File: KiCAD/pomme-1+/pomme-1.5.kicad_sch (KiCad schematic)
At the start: 34 parts, among them J6 clock select, SW1 RESET, U12 74HC138, U2 74HC04, U3 74HC74, U7 74HC00, Y1 3.6864Mhz

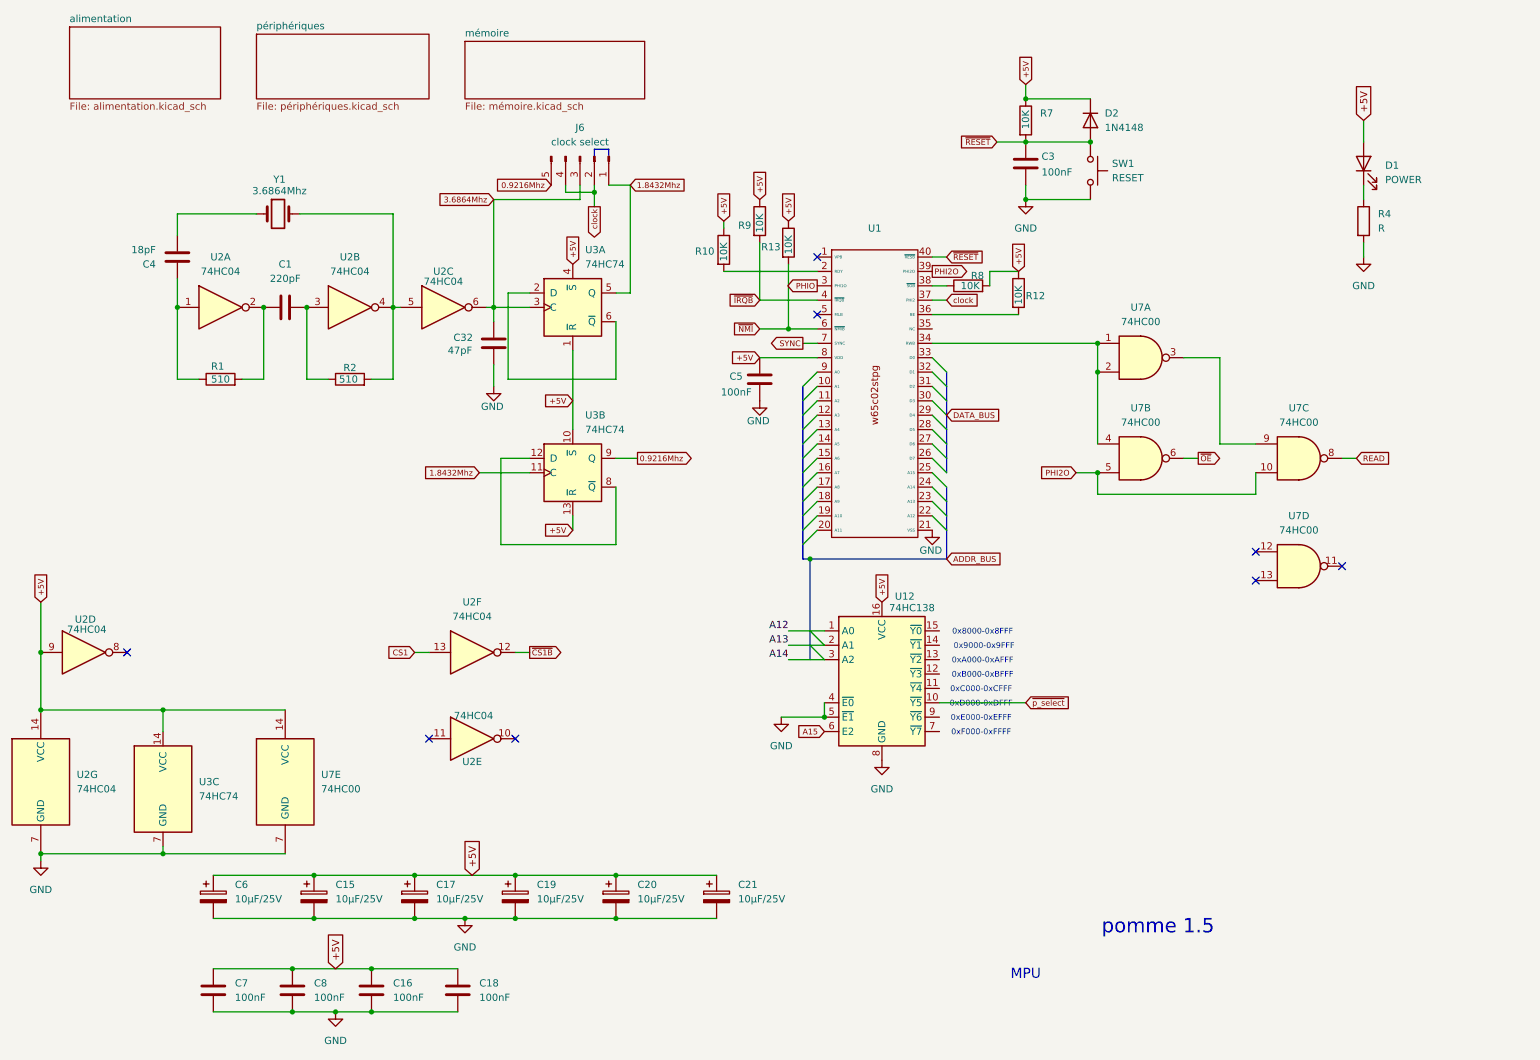
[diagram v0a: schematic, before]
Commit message: Modification de la conception du pomme 1+ Ajout d'un PIA W65C22 à la carte périphériques Ajout d'un régulateur de tension 3.3V à l'alimentation
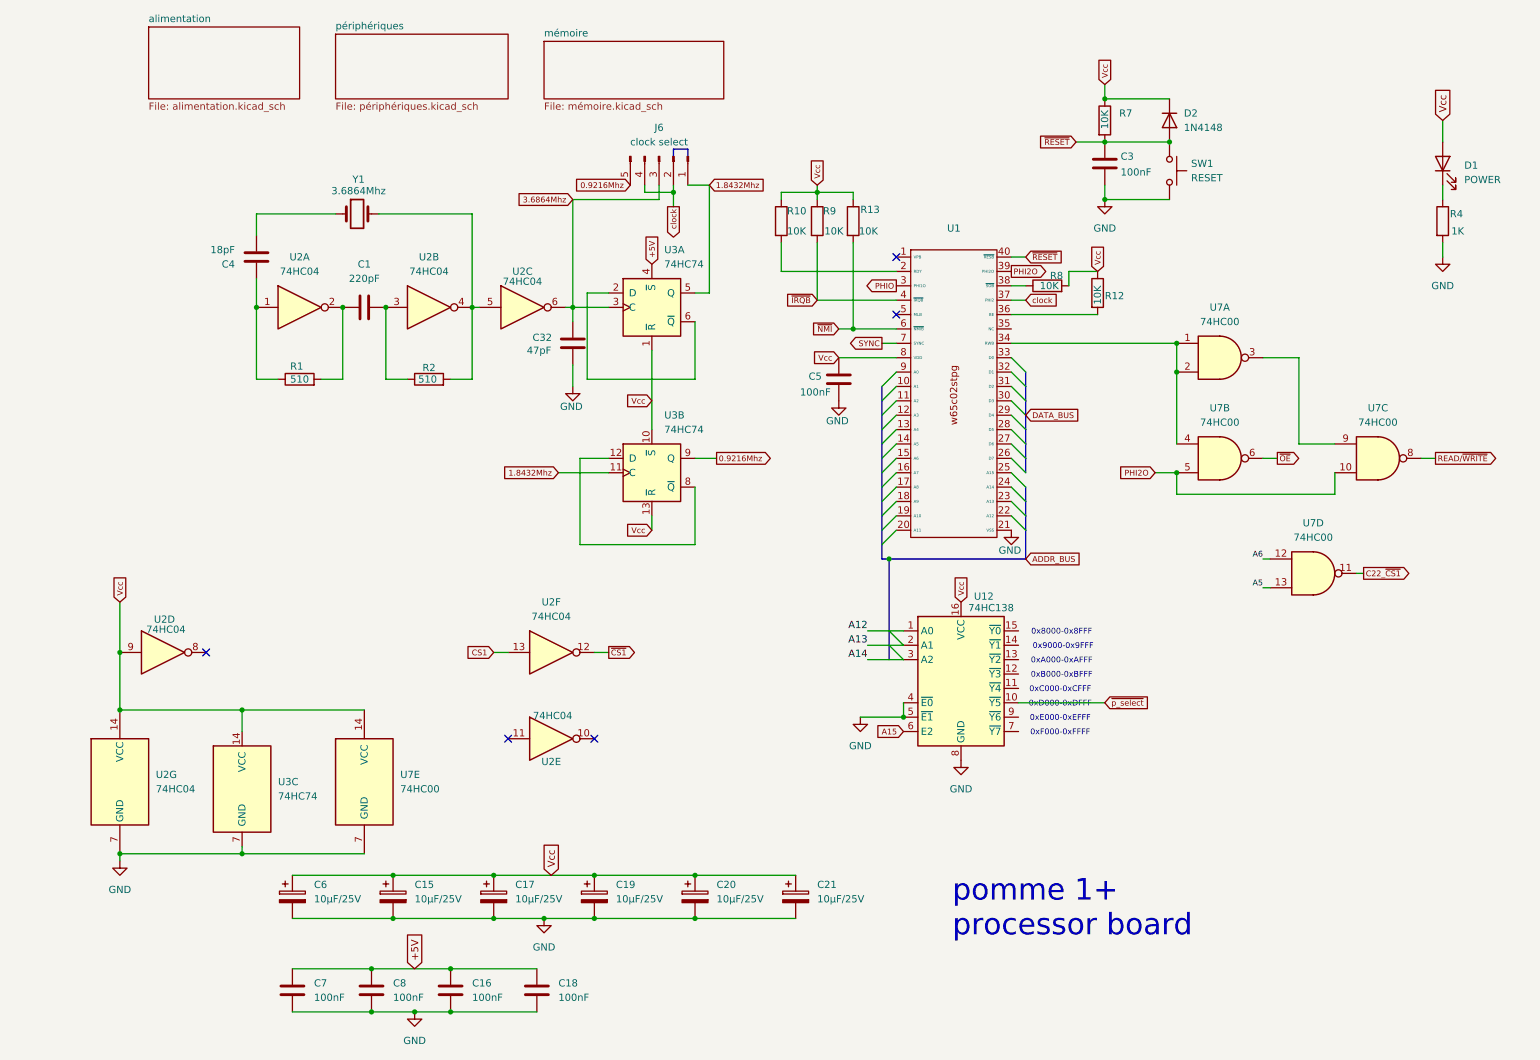
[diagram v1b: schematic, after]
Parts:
- R4: value R -> 1K
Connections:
- net +5V: no longer C15.1, C17.1, C19.1, C20.1, C21.1, C5.1, C6.1, D1.2 (A), D2.1 (K), R10.1, R12.1, R13.1, R7.1, R8.2, R9.1, U1.8 (VDD), U12.16 (VCC), U2.14 (VCC), U2.9, U3.1 (~{R}), U3.10 (~{S}), U3.13 (~{R}), U3.14 (VCC), U7.14 (VCC)
- net C22_~{CS1}: now reaches U7.11
- net A6: now reaches U7.12
- net A5: now reaches U7.13
- net READ renamed READ/~{WRITE}
- net ~{CS1B} renamed ~{CS1}
- new net Vcc: C15.1, C17.1, C19.1, C20.1, C21.1, C5.1, C6.1, D1.2 (A), D2.1 (K), R10.1, R12.1, R13.1, R7.1, R8.2, R9.1, U1.8 (VDD), U12.16 (VCC), U2.14 (VCC), U2.9, U3.1 (~{R}), U3.10 (~{S}), U3.13 (~{R}), U3.14 (VCC), U7.14 (VCC)
- no-connect marks 8 -> 5
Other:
- note added: "pomme 1+ processor board"
- note removed: "MPU"
- note removed: "pomme 1.5"
- moved on the sheet: C1, C15, C16, C17, C18, C19, C20, C21, C3, C32, C4, C5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

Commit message: Modification documents
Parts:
- renumbered C4 to C1, C32 to C10, C19 to C11, C20 to C12, C21 to C13, C5 to C14, C3 to C15, C6 to C2, C7 to C3, C1 to C4, C8 to C5, C15 to C6, C16 to C7, C17 to C8, C18 to C9, D2 to D1, D1 to D2, J6 to J1, R10 to R3, R9 to R4, R13 to R5, R8 to R6, R12 to R7, R7 to R8, R4 to R9, U2 to U1, U3 to U2, U7 to U3, U1 to U4, U12 to U5

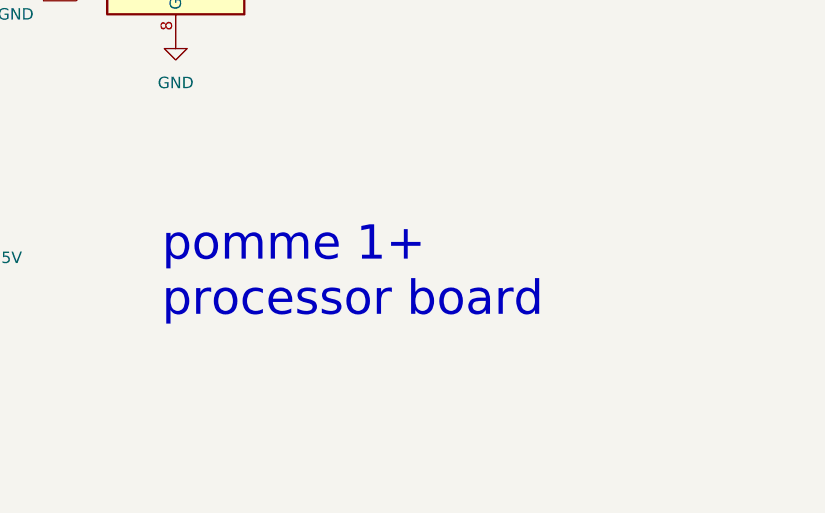
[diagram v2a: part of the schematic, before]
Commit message: Création d'une carte avec mémoire flash W25Q080DV de 1MO pour le stockage des fichiers du pomme 1+
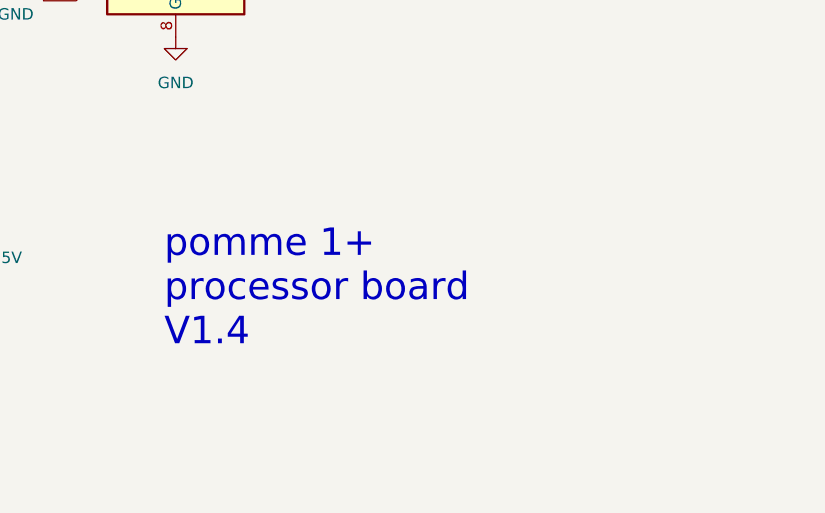
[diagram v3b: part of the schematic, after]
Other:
- note added: "pomme 1+ processor board V1.4"
- note removed: "pomme 1+ processor board"
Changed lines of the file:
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@@
 		)
 	)
-	(text "pomme 1+\nprocessor board\n"
+	(text "pomme 1+\nprocessor board\nV1.4"
 		(exclude_from_sim no)
-		(at 178.816 172.212 0)
+		(at 179.07 173.99 0)
 		(effects
 			(font
-				(size 3.81 3.81)
+				(size 3.048 3.048)
 			)
 			(justify left)

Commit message: Modification schématique V1.5
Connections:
- net C22_~{CS1} renamed C22_~{CS2}
- net ~{CS1} renamed C51_~{CS1}
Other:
- note added: "pomme 1+ processor board V1.5"
- note removed: "pomme 1+ processor board V1.4"
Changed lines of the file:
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@@
 		)
 	)
-	(text "pomme 1+\nprocessor board\nV1.4"
+	(text "pomme 1+\nprocessor board\nV1.5"
 		(exclude_from_sim no)
 		(at 179.07 173.99 0)
@@
 		)
 	)
-	(global_label "C22_~{CS1}"
+	(global_label "C22_~{CS2}"
 		(shape output)
 		(at 251.46 113.03 0)
@@
 		)
 	)
-	(global_label "~{CS1}"
+	(global_label "C51_~{CS1}"
 		(shape output)
 		(at 118.11 127 0)
@@
 		)
 		(property "Intersheetrefs" "${INTERSHEET_REFS}"
-			(at 123.4491 127 0)
-			(effects
-				(font
+			(at 127.1744 127 0)
+			(effects
+				(font

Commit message: Schematic V1.6, modifié circuit pin 12 de U3D pour que la sortie du NAND ne passe à 0 qui si C22_CS1 est à 1
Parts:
- added D7, D8: 1N4148, Diode_THT:D_DO-35_SOD27_P7.62mm_Horizontal, symbol Diode:1N4148
- added R13: 10K, symbol Device:R
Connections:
- net A6: now also D7.1 (K); no longer U3.12
- net Vcc: now also R13.1
- new net: D7.2 (A), D8.2 (A), R13.2, U3.12
- new net C22_CS1: D8.1 (K)
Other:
- note added: "pomme 1+ processor board V1.6"
- note removed: "pomme 1+ processor board V1.5"

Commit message: Correction à la schématique les W65C51S et W65C22S doivent revevoir le signal RWB du mpu plutôt que le signal READ/WRITEB à la pin 8 de U3
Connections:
- net PHI2O: no longer U3.10, U3.5
- net R/~{W}: now reaches U3.1, U3.2, U3.4, U4.34 (RWB)
- new net PHI2: U3.10, U3.5
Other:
- note added: "pomme 1+ processor board V1.8"
- note removed: "pomme 1+ processor board V1.6"
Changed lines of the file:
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@@
+	)
+	(junction
+		(at 200.66 72.39)
+		(diameter 0)
+		(color 0 0 0 0)
 	)
 	(junction
@@
 	(wire
 		(pts
+			(xy 200.66 72.39) (xy 218.44 72.39)
+		)
+		(stroke
+			(width 0)
+			(type default)
+		)
+	)
+	(wire
+		(pts
 			(xy 161.29 69.85) (xy 168.91 69.85)
 		)
@@
 		)
 	)
+	(wire
+		(pts
+			(xy 200.66 72.39) (xy 200.66 74.93)
+		)
+		(stroke
+			(width 0)
+			(type default)
+		)
+	)
 	(bus
 		(pts
@@
 	(wire
 		(pts
-			(xy 189.23 72.39) (xy 218.44 72.39)
+			(xy 189.23 72.39) (xy 200.66 72.39)
 		)
 		(stroke
@@
 		)
 	)
-	(text "pomme 1+\nprocessor board\nV1.6"
+	(text "pomme 1+\nprocessor board\nV1.8"
 		(exclude_from_sim no)
 		(at 179.07 173.99 0)
@@
 		)
 	)
-	(global_label "PHI2O"
+	(global_label "PHI2"
 		(shape input)
 		(at 214.63 95.25 180)
@@
 		)
 		(property "Intersheetrefs" "${INTERSHEET_REFS}"
-			(at 207.6459 95.25 0)
+			(at 208.7103 95.25 0)
 			(effects
 				(font
@@
 				(hide yes)
 			)
+		)
+	)
+	(global_label "R{slash}~{W}"
+		(shape output)
+		(at 200.66 74.93 270)
+		(fields_autoplaced yes)
+		(effects
+			(font
+				(size 1.016 1.016)
+			)
+			(justify right)
+		)
+		(property "Intersheetrefs" "${INTERSHEET_REFS}"
+			(at 200.66 80.5594 90)
+			(effects
+				(font
+					(size 1.27 1.27)
+				)
+				(justify right)
+				(hide yes)
+			)

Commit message: Modification du circuit pour ajouter un amplificateur audio LM4861 sur la carte amovible qui se branche sur le connecteur VIA BUS
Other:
- added sheet carte_ssd_son (carte_ssd_son.kicad_sch)
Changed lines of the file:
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@@
 (kicad_sch
-	(version 20231120)
+	(version 20250114)
 	(generator "eeschema")
-	(generator_version "8.0")
+	(generator_version "9.0")
 	(paper "A4")
+	(text "0x9000-0x9FFF"
+		(exclude_from_sim no)
+		(at 198.374 125.984 0)
+		(effects
+			(font
+				(size 1.016 1.016)
+			)
+		)
+	)
+	(text "pomme 1+\nprocessor board\nV1.8"
+		(exclude_from_sim no)
+		(at 179.07 173.99 0)
+		(effects
+			(font
+				(size 3.048 3.048)
+			)
+			(justify left)
+		)
+	)
+	(text "0xF000-0xFFFF"
+		(exclude_from_sim no)
+		(at 197.866 141.224 0)
+		(effects
+			(font
+				(size 1.016 1.016)
+			)
+		)
+	)
+	(text "0xE000-0xEFFF"
+		(exclude_from_sim no)
+		(at 197.866 138.684 0)
+		(effects
+			(font
+				(size 1.016 1.016)
+			)
+		)
+	)
+	(text "0xD000-0xDFFF"
+		(exclude_from_sim no)
+		(at 197.866 136.144 0)
+		(effects
+			(font
+				(size 1.016 1.016)
+			)
+		)
+	)
+	(text "0xA000-0xAFFF"
+		(exclude_from_sim no)
+		(at 198.12 128.524 0)
+		(effects
+			(font
+				(size 1.016 1.016)
+			)
+		)
+	)
+	(text "0xB000-0xBFFF"
+		(exclude_from_sim no)
+		(at 198.12 131.064 0)
+		(effects
+			(font
+				(size 1.016 1.016)
+			)
+		)
+	)
+	(text "0x8000-0x8FFF"
+		(exclude_from_sim no)
+		(at 198.12 123.444 0)
+		(effects
+			(font
+				(size 1.016 1.016)
+			)
+		)
+	)
+	(text "0xC000-0xCFFF"
+		(exclude_from_sim no)
+		(at 197.866 133.604 0)
+		(effects
+			(font
+				(size 1.016 1.016)
+			)
+		)
+	)
 	(junction
 		(at 161.29 69.85)
@@
 		)
 	)
-	(text "0x9000-0x9FFF"
-		(exclude_from_sim no)
-		(at 198.374 125.984 0)
-		(effects
-			(font
-				(size 1.016 1.016)
-			)
-		)
-	)
-	(text "pomme 1+\nprocessor board\nV1.8"
-		(exclude_from_sim no)
-		(at 179.07 173.99 0)
-		(effects
-			(font
-				(size 3.048 3.048)
-			)
-			(justify left)
-		)
-	)
-	(text "0xF000-0xFFFF"
-		(exclude_from_sim no)
-		(at 197.866 141.224 0)
-		(effects
-			(font
-				(size 1.016 1.016)
-			)
-		)
-	)
-	(text "0xE000-0xEFFF"
-		(exclude_from_sim no)
-		(at 197.866 138.684 0)
-		(effects
-			(font
-				(size 1.016 1.016)
-			)
-		)
-	)
-	(text "0xD000-0xDFFF"
-		(exclude_from_sim no)
-		(at 197.866 136.144 0)
-		(effects
-			(font
-				(size 1.016 1.016)
-			)
-		)
-	)
-	(text "0xA000-0xAFFF"
-		(exclude_from_sim no)
-		(at 198.12 128.524 0)
-		(effects
-			(font
-				(size 1.016 1.016)
-			)
-		)
-	)
-	(text "0xB000-0xBFFF"
-		(exclude_from_sim no)
-		(at 198.12 131.064 0)
-		(effects
-			(font
-				(size 1.016 1.016)
-			)
-		)
-	)
-	(text "0x8000-0x8FFF"
-		(exclude_from_sim no)
-		(at 198.12 123.444 0)
-		(effects
-			(font
-				(size 1.016 1.016)
-			)
-		)
-	)
-	(text "0xC000-0xCFFF"
-		(exclude_from_sim no)
-		(at 197.866 133.604 0)
-		(effects
-			(font
-				(size 1.016 1.016)
-			)
-		)
-	)
 	(label "A6"
 		(at 219.71 110.49 180)
@@
 		(at 36.83 16.51)
 		(size 26.67 12.7)
+		(exclude_from_sim no)
+		(in_bom yes)
+		(on_board yes)
+		(dnp no)
 		(fields_autoplaced yes)
 		(stroke
@@
 		(at 106.68 19.05)
 		(size 31.75 10.16)
+		(exclude_from_sim no)
+		(in_bom yes)
+		(on_board yes)
+		(dnp no)
 		(fields_autoplaced yes)
 		(stroke
@@
 	)
 	(sheet
+		(at 144.018 18.288)
+		(size 27.178 11.938)
+		(exclude_from_sim no)
+		(in_bom yes)
+		(on_board yes)
+		(dnp no)
+		(fields_autoplaced yes)
+		(stroke
+			(width 0.1524)
+			(type solid)
+		)
+		(fill
+			(color 0 0 0 0.0000)
+		)
+		(property "Sheetname" "carte_ssd_son"
+			(at 144.018 17.5764 0)
+			(effects
+				(font
+					(size 1.27 1.27)
+				)
+				(justify left bottom)
+			)
+		)
+		(property "Sheetfile" "carte_ssd_son.kicad_sch"
+			(at 144.018 30.8106 0)
+			(effects
+				(font
+					(size 1.27 1.27)
+				)
+				(justify left top)
+			)
+		)
+		(instances
+			(project "pomme-1.5"
+				(path "/46a37b86-f1f5-4cd9-9809-f219c84ab6f2"
+					(page "5")
+				)
+			)
+		)
+	)
+	(sheet
 		(at 69.85 17.78)
 		(size 30.48 11.43)
+		(exclude_from_sim no)
+		(in_bom yes)
+		(on_board yes)
+		(dnp no)
 		(fields_autoplaced yes)
 		(stroke
@@
 		)
 	)
+	(embedded_fonts no)
 )

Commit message: Modification au circuit du pomme-1+ ajout d'une seconde EEPROM (U13) 0xC000...0xDFFF. Celle-ci peut-être programmée dans le circuit.
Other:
- note added: "pomme 1+ processor board V1.9"
- note removed: "pomme 1+ processor board V1.8"
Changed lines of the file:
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@@
 		)
 	)
-	(text "pomme 1+\nprocessor board\nV1.8"
+	(text "pomme 1+\nprocessor board\nV1.9"
 		(exclude_from_sim no)
 		(at 179.07 173.99 0)
